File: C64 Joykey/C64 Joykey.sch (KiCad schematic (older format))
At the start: 22 parts, among them J1 Port_1, J2 Port_2, M1 Mounting, M2 Mounting, M3 Mounting, M4 Mounting, SW1 FIRE1, SW2 FIRE2, SW3 FIRE3, SW4 UP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

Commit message: Assign footprints
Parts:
- D1, D2, D3, D4: footprint (none) -> Diodes_THT:D_DO-35_SOD27_P7.62mm_Horizontal
- J1, J2: footprint (none) -> Pin_Headers:Pin_Header_Straight_2x05_Pitch2.54mm
- JP1, JP2, JP3: footprint (none) -> Pin_Headers:Pin_Header_Straight_1x03_Pitch2.54mm
- M1, M2, M3, M4: footprint (none) -> mounting:M3
- R1, R2: footprint (none) -> Resistors_THT:R_Axial_DIN0207_L6.3mm_D2.5mm_P7.62mm_Horizontal
- SW1, SW2, SW3, SW4, SW5, SW6, SW7: footprint (none) -> Button_Switch_Keyboard:SW_Cherry_MX_1.00u_PCB
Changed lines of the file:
@@
 F 0 "M1" H 10700 650 50  0001 C CNN
 F 1 "Mounting" H 10700 475 50  0001 C CNN
-F 2 "" H 10700 550 50  0001 C CNN
+F 2 "mounting:M3" H 10700 550 50  0001 C CNN
 F 3 "~" H 10700 550 50  0001 C CNN
 	1    10700 550
@@
 F 0 "M2" H 10825 650 50  0001 C CNN
 F 1 "Mounting" H 10825 475 50  0001 C CNN
-F 2 "" H 10825 550 50  0001 C CNN
+F 2 "mounting:M3" H 10825 550 50  0001 C CNN
 F 3 "~" H 10825 550 50  0001 C CNN
 	1    10825 550
@@
 F 0 "M3" H 10975 650 50  0001 C CNN
 F 1 "Mounting" H 10975 475 50  0001 C CNN
-F 2 "" H 10975 550 50  0001 C CNN
+F 2 "mounting:M3" H 10975 550 50  0001 C CNN
 F 3 "~" H 10975 550 50  0001 C CNN
 	1    10975 550
@@
 F 0 "M4" H 11100 650 50  0001 C CNN
 F 1 "Mounting" H 11100 475 50  0001 C CNN
-F 2 "" H 11100 550 50  0001 C CNN
+F 2 "mounting:M3" H 11100 550 50  0001 C CNN
 F 3 "~" H 11100 550 50  0001 C CNN
 	1    11100 550
@@
 F 0 "SW1" V 2644 1227 50  0000 C CNN
 F 1 "FIRE1" V 2735 1227 50  0000 C CNN
-F 2 "" H 2950 1425 50  0001 C CNN
+F 2 "Button_Switch_Keyboard:SW_Cherry_MX_1.00u_PCB" H 2950 1425 50  0001 C CNN
 F 3 "" H 2950 1425 50  0001 C CNN
 	1    2950 1225
@@
 F 0 "SW2" V 2644 2402 50  0000 C CNN
 F 1 "FIRE2" V 2735 2402 50  0000 C CNN
-F 2 "" H 2950 2600 50  0001 C CNN
+F 2 "Button_Switch_Keyboard:SW_Cherry_MX_1.00u_PCB" H 2950 2600 50  0001 C CNN
 F 3 "" H 2950 2600 50  0001 C CNN
 	1    2950 2400
@@
 F 0 "SW3" V 2644 4052 50  0000 C CNN
 F 1 "FIRE3" V 2735 4052 50  0000 C CNN
-F 2 "" H 2950 4250 50  0001 C CNN
+F 2 "Button_Switch_Keyboard:SW_Cherry_MX_1.00u_PCB" H 2950 4250 50  0001 C CNN
 F 3 "" H 2950 4250 50  0001 C CNN
 	1    2950 4050
@@
 F 0 "J2" H 9050 3217 50  0000 C CNN
 F 1 "Port_2" H 9050 3126 50  0000 C CNN
-F 2 "" H 9000 2800 50  0001 C CNN
+F 2 "Pin_Headers:Pin_Header_Straight_2x05_Pitch2.54mm" H 9000 2800 50  0001 C CNN
 F 3 "~" H 9000 2800 50  0001 C CNN
 	1    9000 2800
@@
 F 0 "J1" H 9050 4017 50  0000 C CNN
 F 1 "Port_1" H 9050 3926 50  0000 C CNN
-F 2 "" H 9000 3600 50  0001 C CNN
+F 2 "Pin_Headers:Pin_Header_Straight_2x05_Pitch2.54mm" H 9000 3600 50  0001 C CNN
 F 3 "~" H 9000 3600 50  0001 C CNN
 	1    9000 3600
@@
 F 0 "SW4" V 644 2827 50  0000 C CNN
 F 1 "UP" V 735 2827 50  0000 C CNN
-F 2 "" H 950 3025 50  0001 C CNN
+F 2 "Button_Switch_Keyboard:SW_Cherry_MX_1.00u_PCB" H 950 3025 50  0001 C CNN
 F 3 "" H 950 3025 50  0001 C CNN
 	1    950  2825
@@
 F 0 "SW5" V 644 3402 50  0000 C CNN
 F 1 "DOWN" V 735 3402 50  0000 C CNN
-F 2 "" H 950 3600 50  0001 C CNN
+F 2 "Button_Switch_Keyboard:SW_Cherry_MX_1.00u_PCB" H 950 3600 50  0001 C CNN
 F 3 "" H 950 3600 50  0001 C CNN
 	1    950  3400
@@
 F 0 "SW6" V 644 3977 50  0000 C CNN
 F 1 "LEFT" V 735 3977 50  0000 C CNN
-F 2 "" H 950 4175 50  0001 C CNN
+F 2 "Button_Switch_Keyboard:SW_Cherry_MX_1.00u_PCB" H 950 4175 50  0001 C CNN
 F 3 "" H 950 4175 50  0001 C CNN
 	1    950  3975
@@
 F 0 "SW7" V 644 4552 50  0000 C CNN
 F 1 "RIGHT" V 735 4552 50  0000 C CNN
-F 2 "" H 950 4750 50  0001 C CNN
+F 2 "Button_Switch_Keyboard:SW_Cherry_MX_1.00u_PCB" H 950 4750 50  0001 C CNN
 F 3 "" H 950 4750 50  0001 C CNN
 	1    950  4550
@@
 F 0 "JP1" H 2775 3286 50  0000 C CNN
 F 1 "F2_COM" H 2775 3377 50  0000 C CNN
-F 2 "" H 2775 3175 50  0001 C CNN
+F 2 "Pin_Headers:Pin_Header_Straight_1x03_Pitch2.54mm" H 2775 3175 50  0001 C CNN
 F 3 "~" H 2775 3175 50  0001 C CNN
 	1    2775 3175
@@
 F 0 "R1" H 2834 2896 50  0000 L CNN
 F 1 "270" H 2834 2805 50  0000 L CNN
-F 2 "" H 2775 2850 50  0001 C CNN
+F 2 "Resistors_THT:R_Axial_DIN0207_L6.3mm_D2.5mm_P7.62mm_Horizontal" H 2775 2850 50  0001 C CNN
 F 3 "~" H 2775 2850 50  0001 C CNN
 	1    2775 2850
@@
 F 0 "D1" H 1300 2905 50  0000 C CNN
 F 1 "1n4148" H 1300 2814 50  0000 C CNN
-F 2 "" V 1300 2700 50  0001 C CNN
+F 2 "Diodes_THT:D_DO-35_SOD27_P7.62mm_Horizontal" V 1300 2700 50  0001 C CNN
 F 3 "~" V 1300 2700 50  0001 C CNN
 	1    1300 2700
@@
 F 0 "D2" H 1300 3480 50  0000 C CNN
 F 1 "1n4148" H 1300 3389 50  0000 C CNN
-F 2 "" V 1300 3275 50  0001 C CNN
+F 2 "Diodes_THT:D_DO-35_SOD27_P7.62mm_Horizontal" V 1300 3275 50  0001 C CNN
 F 3 "~" V 1300 3275 50  0001 C CNN
 	1    1300 3275
@@
 F 0 "D3" H 1300 4055 50  0000 C CNN
 F 1 "1n4148" H 1300 3964 50  0000 C CNN
-F 2 "" V 1300 3850 50  0001 C CNN
+F 2 "Diodes_THT:D_DO-35_SOD27_P7.62mm_Horizontal" V 1300 3850 50  0001 C CNN
 F 3 "~" V 1300 3850 50  0001 C CNN
 	1    1300 3850
@@
 F 0 "D4" H 1300 4630 50  0000 C CNN
 F 1 "1n4148" H 1300 4539 50  0000 C CNN
-F 2 "" V 1300 4425 50  0001 C CNN
+F 2 "Diodes_THT:D_DO-35_SOD27_P7.62mm_Horizontal" V 1300 4425 50  0001 C CNN
 F 3 "~" V 1300 4425 50  0001 C CNN
 	1    1300 4425
@@
 F 0 "JP3" H 3575 4261 50  0000 C CNN
 F 1 "FIRE3_SEL" H 3575 4352 50  0000 C CNN
-F 2 "" H 3575 4150 50  0001 C CNN
+F 2 "Pin_Headers:Pin_Header_Straight_1x03_Pitch2.54mm" H 3575 4150 50  0001 C CNN
 F 3 "~" H 3575 4150 50  0001 C CNN
 	1    3575 4150
@@
 F 0 "JP2" H 2775 4936 50  0000 C CNN
 F 1 "F3_COM" H 2775 5027 50  0000 C CNN
-F 2 "" H 2775 4825 50  0001 C CNN
+F 2 "Pin_Headers:Pin_Header_Straight_1x03_Pitch2.54mm" H 2775 4825 50  0001 C CNN
 F 3 "~" H 2775 4825 50  0001 C CNN
 	1    2775 4825
@@
 F 0 "R2" H 2834 4546 50  0000 L CNN
 F 1 "270" H 2834 4455 50  0000 L CNN
-F 2 "" H 2775 4500 50  0001 C CNN
+F 2 "Resistors_THT:R_Axial_DIN0207_L6.3mm_D2.5mm_P7.62mm_Horizontal" H 2775 4500 50  0001 C CNN
 F 3 "~" H 2775 4500 50  0001 C CNN
 	1    2775 4500

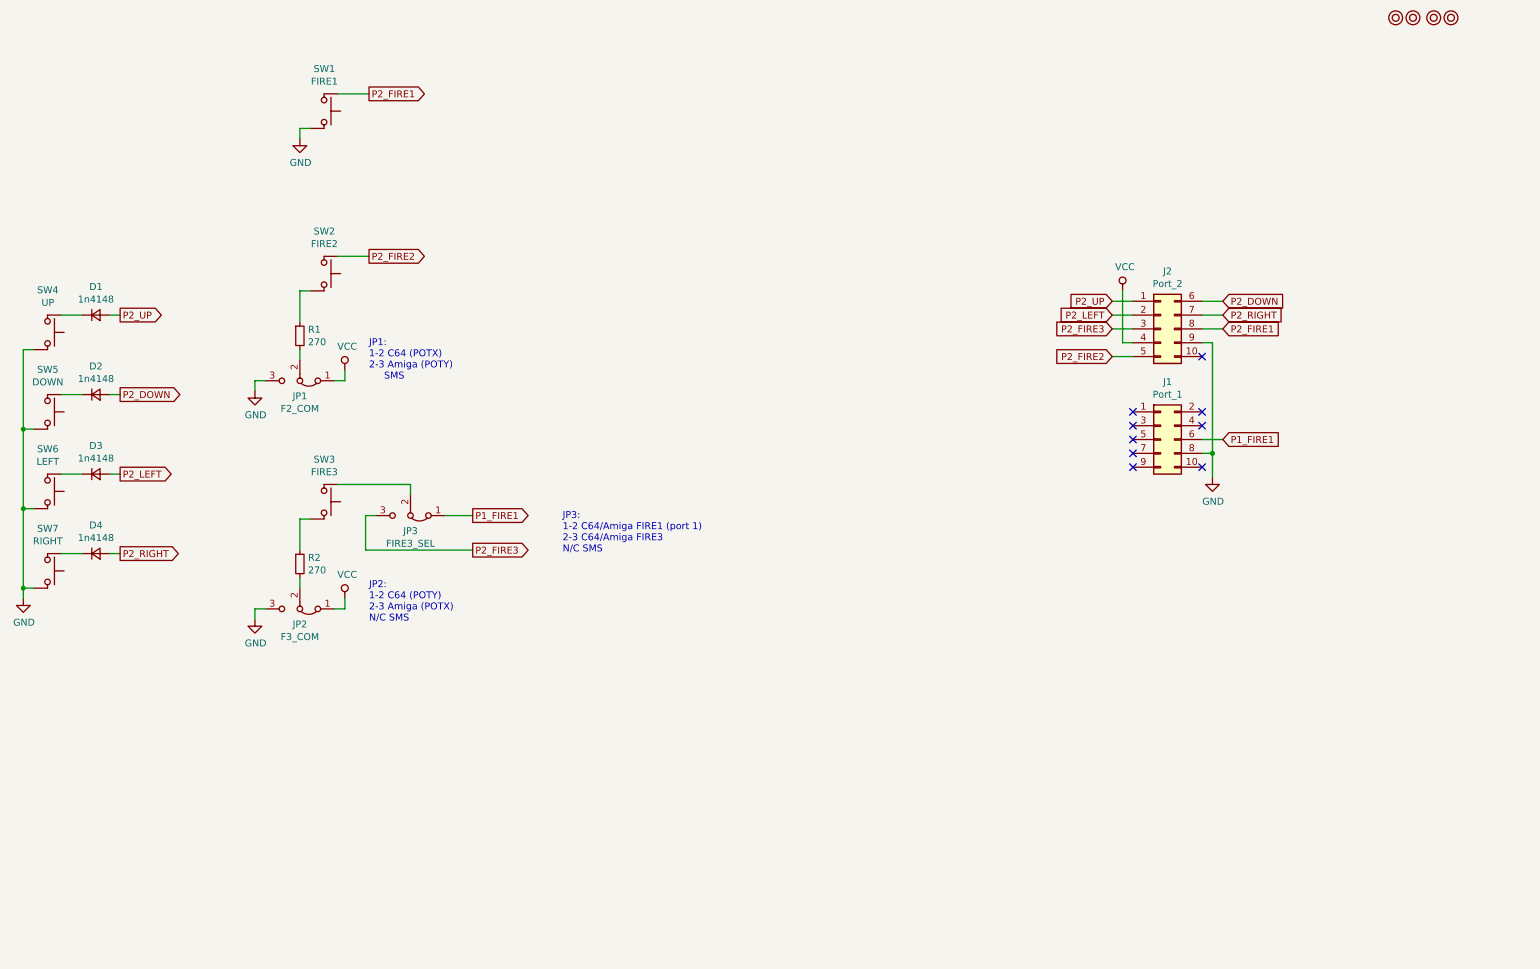
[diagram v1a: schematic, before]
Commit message: Rough placement
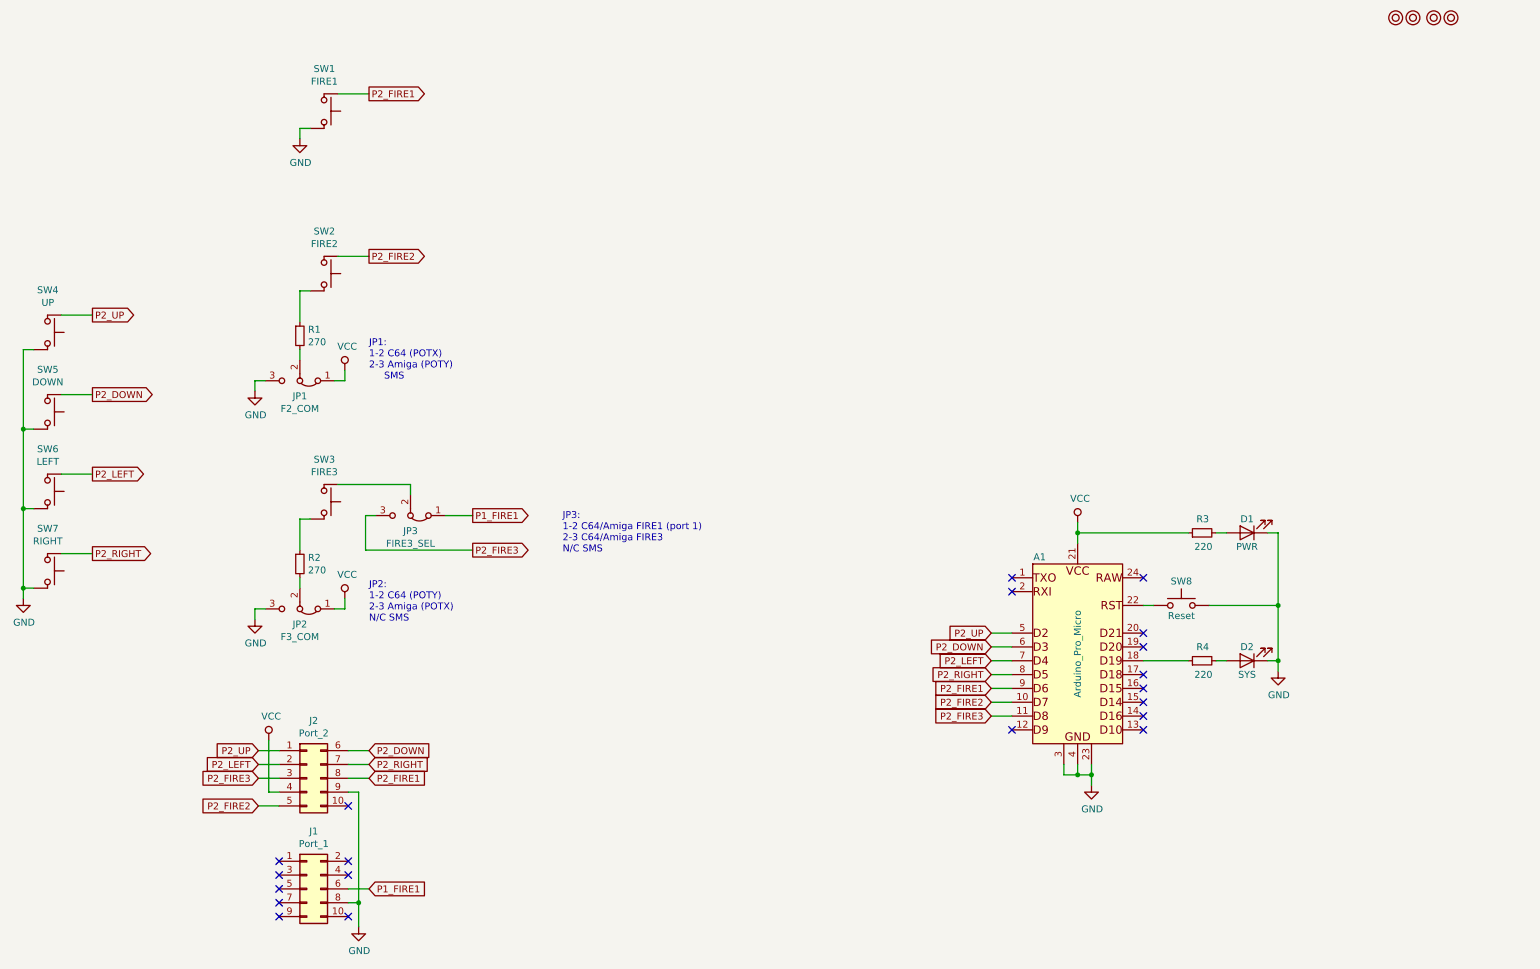
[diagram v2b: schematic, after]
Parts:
- removed D1, D2, D3, D4: 1n4148, Diodes_THT:D_DO-35_SOD27_P7.62mm_Horizontal, symbol Device:D_Small
- added A1: Arduino_Pro_Micro, arduino_pro_micro:Arduino_Pro_Micro, symbol promicro:Arduino_Pro_Micro
- added D1: PWR, LEDs:LED_D5.0mm, symbol Device:LED
- added D2: SYS, LEDs:LED_D5.0mm, symbol Device:LED
- added R3, R4: 220, Resistors_THT:R_Axial_DIN0207_L6.3mm_D2.5mm_P7.62mm_Horizontal, symbol Device:R_Small
- added SW8: Reset, Buttons_Switches_THT:SW_PUSH_6mm, symbol Switch:SW_Push
- J1, J2: footprint Pin_Headers:Pin_Header_Straight_2x05_Pitch2.54mm -> Connector_IDC:IDC-Header_2x05_P2.54mm_Vertical
- JP1, JP2, JP3: footprint Pin_Headers:Pin_Header_Straight_1x03_Pitch2.54mm -> Pin_Headers:Pin_Header_Angled_1x03_Pitch2.54mm
- M1, M2, M3, M4: footprint mounting:M3 -> mounting:M3_pin
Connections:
- net GND: now also A1.23 (GND), A1.3 (GND), A1.4 (GND), D1.1 (K), D2.1 (K), SW8.2
- net P2_DOWN: now also SW5.1, A1.6 (D3)
- net P2_FIRE1: now also A1.9 (D6)
- net P2_FIRE2: now also A1.10 (D7)
- net P2_FIRE3: now also A1.11 (D8)
- net P2_LEFT: now also SW6.1, A1.7 (D4)
- net P2_RIGHT: now also SW7.1, A1.8 (D5)
- net P2_UP: now also SW4.1, A1.5 (D2)
- net VCC: now also A1.21 (VCC), R3.1
- new net: A1.18 (D19), R4.1
- new net: A1.22 (RST), SW8.1
- new net: D1.2 (A), R3.2
- new net: D2.2 (A), R4.2
- no-connect marks 9 -> 20
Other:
- moved on the sheet: J1, J2

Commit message: Routed tracks
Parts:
- added JP4: DEFAULT_FW, Pin_Headers:Pin_Header_Straight_1x02_Pitch2.54mm, symbol Device:Jumper_NC_Small
- J1: footprint Connector_IDC:IDC-Header_2x05_P2.54mm_Vertical -> C64 IDC:IDC_Joystick; symbol Connector_Generic:Conn_02x05_Odd_Even -> Connector_Generic:Conn_02x05_Top_Bottom
- J2: footprint Connector_IDC:IDC-Header_2x05_P2.54mm_Vertical -> C64 IDC:IDC_Joystick
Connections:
- net GND: now also J2.8 (Pin_8); no longer J2.9 (Pin_9)
- net P2_DOWN: now also A1.14 (D16), J2.2 (Pin_2); no longer A1.6 (D3), J2.6 (Pin_6)
- net P2_FIRE1: now also A1.8 (D5), J2.6 (Pin_6), JP4.2; no longer A1.9 (D6), J2.8 (Pin_8), SW1.1
- net P2_FIRE2: now also A1.6 (D3), J2.9 (Pin_9); no longer A1.10 (D7), J2.5 (Pin_5)
- net P2_FIRE3: now also J2.5 (Pin_5); no longer A1.11 (D8), J2.3 (Pin_3)
- net P2_LEFT: now also A1.13 (D10), J2.3 (Pin_3); no longer A1.7 (D4), J2.2 (Pin_2)
- net P2_RIGHT: now also A1.15 (D14), J2.4 (Pin_4); no longer A1.8 (D5), J2.7 (Pin_7)
- net P2_UP: now also A1.16 (D15); no longer A1.5 (D2)
- net VCC: now also J2.7 (Pin_7); no longer J2.4 (Pin_4)
- net FIRE2_POL: now reaches R1.1, SW2.2
- net FIRE2_POL: now also A1.9 (D6)
- net FIRE3_IN: now reaches JP3.2 (C), SW3.1
- net FIRE3_IN: now also A1.7 (D4)
- net FIRE3_POL: now reaches R2.1, SW3.2
- net FIRE3_POL: now also A1.10 (D7)
- new net FIRE1_IN: A1.5 (D2), JP4.1, SW1.1
- no-connect marks 20 -> 17
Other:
- note added: "Experimental feature to have Arduino act\nas an autofire, but needs to be wired\nspecificly in order to not fry pro micro\noutput pin."
- note added: "JP1 (fire2 polarity):\n1-2 C64 (POTX)\n2-3 Amiga (POTY)\n SMS\n"
- note added: "JP2 (fire3 polarity):\n1-2 C64 (POTY)\n2-3 Amiga (POTX)\nN/C SMS\n"
- note added: "JP3 (fire3 wiring):\n1-2 C64/Amiga FIRE1 (port 1)\n2-3 C64/Amiga FIRE3 (port 2)\nN/C SMS/Arduino"
- note removed: "JP1:\n1-2 C64 (POTX)\n2-3 Amiga (POTY)\n SMS\n"
- note removed: "JP2:\n1-2 C64 (POTY)\n2-3 Amiga (POTX)\nN/C SMS\n"
- note removed: "JP3:\n1-2 C64/Amiga FIRE1 (port 1)\n2-3 C64/Amiga FIRE3\nN/C SMS"
- moved on the sheet: J1, J2, JP2, R2
